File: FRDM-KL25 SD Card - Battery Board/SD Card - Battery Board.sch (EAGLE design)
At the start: 59 parts, among them U1 TPS63001, U2 TPS63002, U3 BQ27510DRZT-G3, U4 BQ24210DQCT

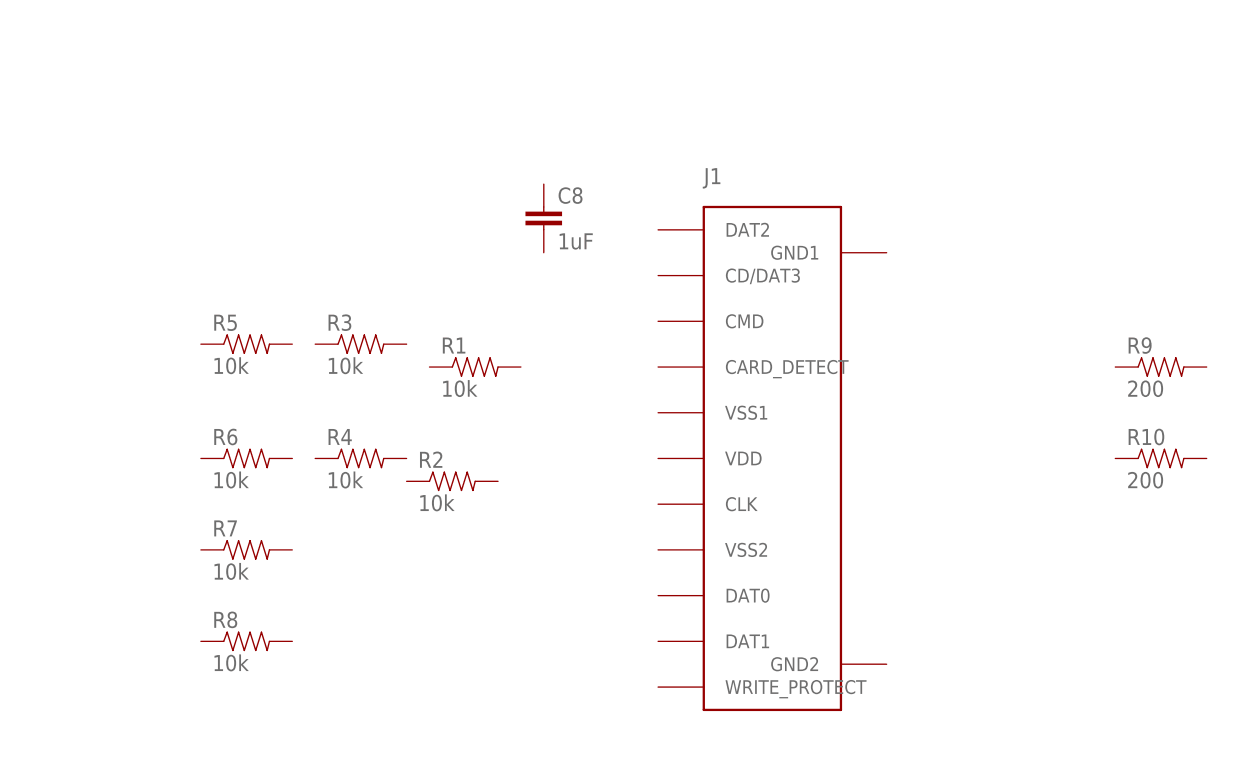
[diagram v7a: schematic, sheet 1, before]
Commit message: FRDM-KL25Z: Conected SD card circuit, nets have not been named
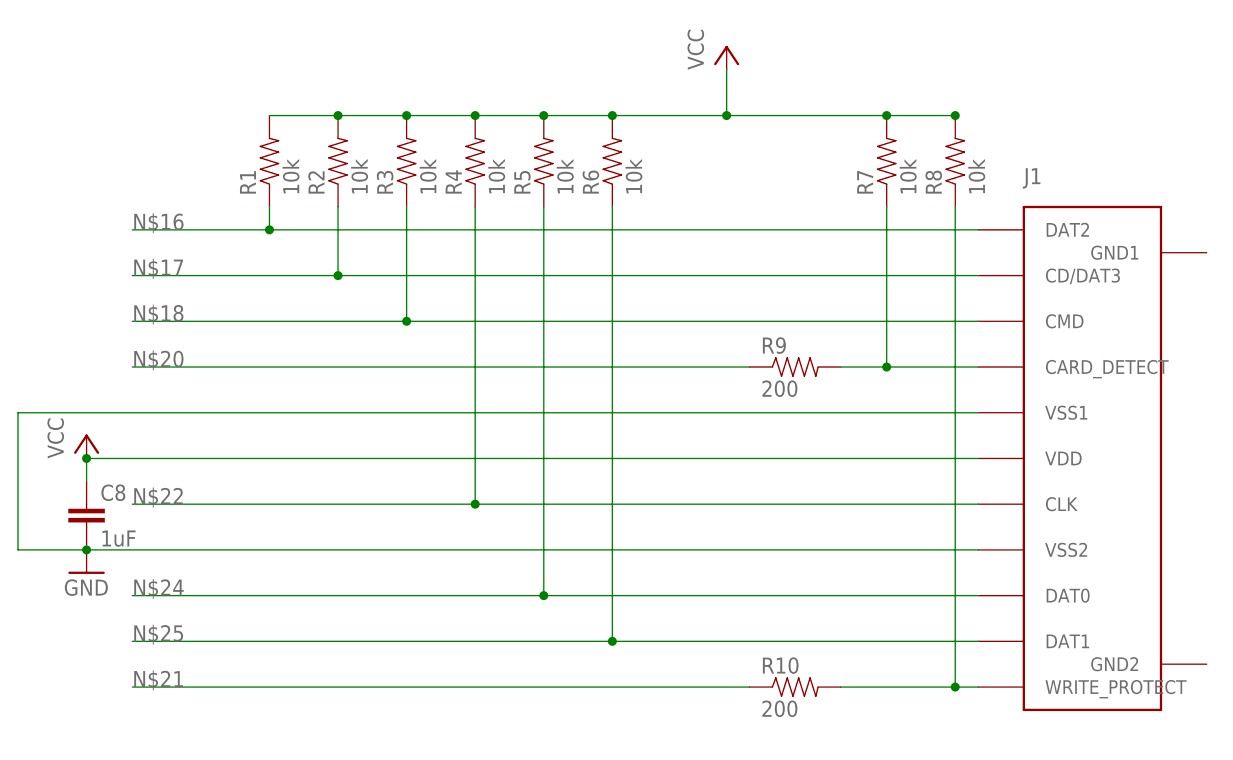
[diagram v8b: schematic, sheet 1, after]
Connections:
- new net N$16: J1.DAT2, R1.1
- new net N$17: J1.CD/DAT3, R2.1
- new net N$18: J1.CMD, R3.1
- new net N$19: J1.CARD_DETECT, R7.1, R9.2
- new net N$20: R9.1
- new net N$21: R10.1
- new net N$22: J1.CLK, R4.1
- new net N$24: J1.DAT0, R5.1
- new net N$25: J1.DAT1, R6.1
- new net N$26: J1.WRITE_PROTECT, R10.2, R8.1
- new net VCC: C8.1, J1.VDD, R1.2, R2.2, R3.2, R4.2, R5.2, R6.2, R7.2, R8.2
- net GND: now also C8.2, J1.VSS1, J1.VSS2
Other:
- moved on the sheet: C8, J1, R1, R10, R2, R3, R4, R5, R6, R7, R8, R9
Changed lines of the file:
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@@
 <part name="C13" library="Kas-Capacitors" deviceset="CAPACITOR" device="0.1U-X7R-10%-25V-0603" value="0.1uF"/>
 <part name="C14" library="Kas-Capacitors" deviceset="CAPACITOR" device="0.1U-X7R-10%-25V-0603" value="0.1uF"/>
+<part name="GND4" library="Kas-Pwr" deviceset="GND" device=""/>
+<part name="P+1" library="Kas-Pwr" deviceset="VCC" device=""/>
+<part name="P+2" library="Kas-Pwr" deviceset="VCC" device=""/>
 </parts>
 <sheets>
@@
 </plain>
 <instances>
-<instance part="R1" gate="G$1" x="25.4" y="63.5"/>
-<instance part="R2" gate="G$1" x="22.86" y="50.8"/>
-<instance part="R3" gate="G$1" x="12.7" y="66.04"/>
-<instance part="R4" gate="G$1" x="12.7" y="53.34"/>
-<instance part="R5" gate="G$1" x="0" y="66.04"/>
-<instance part="R6" gate="G$1" x="0" y="53.34"/>
-<instance part="R7" gate="G$1" x="0" y="43.18"/>
-<instance part="R8" gate="G$1" x="0" y="33.02"/>
-<instance part="R9" gate="G$1" x="101.6" y="63.5"/>
-<instance part="R10" gate="G$1" x="101.6" y="53.34"/>
-<instance part="J1" gate="G$1" x="58.42" y="58.42"/>
-<instance part="C8" gate="G$1" x="33.02" y="78.74"/>
+<instance part="R1" gate="G$1" x="2.54" y="86.36" rot="R90"/>
+<instance part="R2" gate="G$1" x="10.16" y="86.36" rot="R90"/>
+<instance part="R3" gate="G$1" x="17.78" y="86.36" rot="R90"/>
+<instance part="R4" gate="G$1" x="25.4" y="86.36" rot="R90"/>
+<instance part="R5" gate="G$1" x="33.02" y="86.36" rot="R90"/>
+<instance part="R6" gate="G$1" x="40.64" y="86.36" rot="R90"/>
+<instance part="R7" gate="G$1" x="71.12" y="86.36" rot="R90"/>
+<instance part="R8" gate="G$1" x="78.74" y="86.36" rot="R90"/>
+<instance part="R9" gate="G$1" x="60.96" y="63.5"/>
+<instance part="R10" gate="G$1" x="60.96" y="27.94"/>
+<instance part="J1" gate="G$1" x="93.98" y="58.42"/>
+<instance part="C8" gate="G$1" x="-17.78" y="45.72"/>
+<instance part="GND4" gate="1" x="-17.78" y="40.64"/>
+<instance part="P+1" gate="VCC" x="-17.78" y="55.88"/>
+<instance part="P+2" gate="VCC" x="53.34" y="99.06"/>
 </instances>
 <busses>
 </busses>
 <nets>
+<net name="N$16" class="0">
+<segment>
+<pinref part="J1" gate="G$1" pin="DAT2"/>
+<wire x1="81.28" y1="78.74" x2="2.54" y2="78.74" width="0.1524" layer="91"/>
+<pinref part="R1" gate="G$1" pin="1"/>
+<wire x1="2.54" y1="81.28" x2="2.54" y2="78.74" width="0.1524" layer="91"/>
+<junction x="2.54" y="78.74"/>
+<wire x1="2.54" y1="78.74" x2="-10.16" y2="78.74" width="0.1524" layer="91"/>
+<wire x1="-12.7" y1="78.74" x2="-10.16" y2="78.74" width="0.1524" layer="91"/>
+<label x="-12.7" y="78.74" size="1.778" layer="95"/>
+</segment>
+</net>
+<net name="N$17" class="0">
+<segment>
+<pinref part="J1" gate="G$1" pin="CD/DAT3"/>
+<wire x1="81.28" y1="73.66" x2="10.16" y2="73.66" width="0.1524" layer="91"/>
+<pinref part="R2" gate="G$1" pin="1"/>
+<wire x1="10.16" y1="73.66" x2="-12.7" y2="73.66" width="0.1524" layer="91"/>
+<wire x1="10.16" y1="81.28" x2="10.16" y2="73.66" width="0.1524" layer="91"/>
+<junction x="10.16" y="73.66"/>
+<label x="-12.7" y="73.66" size="1.778" layer="95"/>
+</segment>
+</net>
+<net name="N$18" class="0">
+<segment>
+<pinref part="J1" gate="G$1" pin="CMD"/>
+<wire x1="81.28" y1="68.58" x2="17.78" y2="68.58" width="0.1524" layer="91"/>
+<pinref part="R3" gate="G$1" pin="1"/>
+<wire x1="17.78" y1="68.58" x2="-12.7" y2="68.58" width="0.1524" layer="91"/>
+<wire x1="17.78" y1="81.28" x2="17.78" y2="68.58" width="0.1524" layer="91"/>
+<junction x="17.78" y="68.58"/>
+<label x="-12.7" y="68.58" size="1.778" layer="95"/>
+</segment>
+</net>
+<net name="N$19" class="0">
+<segment>
+<pinref part="J1" gate="G$1" pin="CARD_DETECT"/>
+<wire x1="81.28" y1="63.5" x2="71.12" y2="63.5" width="0.1524" layer="91"/>
+<pinref part="R9" gate="G$1" pin="2"/>
+<pinref part="R7" gate="G$1" pin="1"/>
+<wire x1="71.12" y1="63.5" x2="66.04" y2="63.5" width="0.1524" layer="91"/>
+<wire x1="71.12" y1="81.28" x2="71.12" y2="63.5" width="0.1524" layer="91"/>
+<junction x="71.12" y="63.5"/>
+</segment>
+</net>
+<net name="N$22" class="0">
+<segment>
+<pinref part="J1" gate="G$1" pin="CLK"/>
+<wire x1="81.28" y1="48.26" x2="25.4" y2="48.26" width="0.1524" layer="91"/>
+<pinref part="R4" gate="G$1" pin="1"/>
+<wire x1="25.4" y1="48.26" x2="-12.7" y2="48.26" width="0.1524" layer="91"/>
+<wire x1="25.4" y1="81.28" x2="25.4" y2="48.26" width="0.1524" layer="91"/>
+<junction x="25.4" y="48.26"/>
+<label x="-12.7" y="48.26" size="1.778" layer="95"/>
+</segment>
+</net>
+<net name="N$24" class="0">
+<segment>
+<pinref part="J1" gate="G$1" pin="DAT0"/>
+<wire x1="81.28" y1="38.1" x2="33.02" y2="38.1" width="0.1524" layer="91"/>
+<pinref part="R5" gate="G$1" pin="1"/>
+<wire x1="33.02" y1="38.1" x2="-12.7" y2="38.1" width="0.1524" layer="91"/>
+<wire x1="33.02" y1="81.28" x2="33.02" y2="38.1" width="0.1524" layer="91"/>
+<junction x="33.02" y="38.1"/>
+<label x="-12.7" y="38.1" size="1.778" layer="95"/>
+</segment>
+</net>
+<net name="N$25" class="0">
+<segment>
+<pinref part="J1" gate="G$1" pin="DAT1"/>
+<wire x1="81.28" y1="33.02" x2="40.64" y2="33.02" width="0.1524" layer="91"/>
+<pinref part="R6" gate="G$1" pin="1"/>
+<wire x1="40.64" y1="33.02" x2="-12.7" y2="33.02" width="0.1524" layer="91"/>
+<wire x1="40.64" y1="81.28" x2="40.64" y2="33.02" width="0.1524" layer="91"/>
+<junction x="40.64" y="33.02"/>
+<label x="-12.7" y="33.02" size="1.778" layer="95"/>
+</segment>
+</net>
+<net name="N$26" class="0">
+<segment>
+<pinref part="J1" gate="G$1" pin="WRITE_PROTECT"/>
+<wire x1="81.28" y1="27.94" x2="78.74" y2="27.94" width="0.1524" layer="91"/>
+<pinref part="R10" gate="G$1" pin="2"/>
+<pinref part="R8" gate="G$1" pin="1"/>
+<wire x1="78.74" y1="27.94" x2="66.04" y2="27.94" width="0.1524" layer="91"/>
+<wire x1="78.74" y1="81.28" x2="78.74" y2="27.94" width="0.1524" layer="91"/>
+<junction x="78.74" y="27.94"/>
+</segment>
+</net>
+<net name="GND" class="0">
+<segment>
+<pinref part="J1" gate="G$1" pin="VSS1"/>
+<wire x1="81.28" y1="58.42" x2="-25.4" y2="58.42" width="0.1524" layer="91"/>
+<wire x1="-25.4" y1="58.42" x2="-25.4" y2="43.18" width="0.1524" layer="91"/>
+<pinref part="J1" gate="G$1" pin="VSS2"/>
+<wire x1="81.28" y1="43.18" x2="-17.78" y2="43.18" width="0.1524" layer="91"/>
+<pinref part="C8" gate="G$1" pin="2"/>
+<wire x1="-25.4" y1="43.18" x2="-17.78" y2="43.18" width="0.1524" layer="91"/>
+<junction x="-17.78" y="43.18"/>
+<pinref part="GND4" gate="1" pin="GND"/>
+</segment>
+</net>
+<net name="VCC" class="0">
+<segment>
+<pinref part="J1" gate="G$1" pin="VDD"/>
+<wire x1="81.28" y1="53.34" x2="-17.78" y2="53.34" width="0.1524" layer="91"/>
+<pinref part="C8" gate="G$1" pin="1"/>
+<wire x1="-17.78" y1="53.34" x2="-17.78" y2="50.8" width="0.1524" layer="91"/>
+<pinref part="P+1" gate="VCC" pin="VCC"/>
+<junction x="-17.78" y="53.34"/>
+</segment>
+<segment>
+<pinref part="R1" gate="G$1" pin="2"/>
+<pinref part="R8" gate="G$1" pin="2"/>
+<wire x1="2.54" y1="91.44" x2="10.16" y2="91.44" width="0.1524" layer="91"/>
+<pinref part="R2" gate="G$1" pin="2"/>
+<junction x="10.16" y="91.44"/>
+<wire x1="10.16" y1="91.44" x2="17.78" y2="91.44" width="0.1524" layer="91"/>
+<pinref part="R3" gate="G$1" pin="2"/>
+<junction x="17.78" y="91.44"/>
+<wire x1="17.78" y1="91.44" x2="25.4" y2="91.44" width="0.1524" layer="91"/>
+<pinref part="R4" gate="G$1" pin="2"/>
+<junction x="25.4" y="91.44"/>
+<wire x1="25.4" y1="91.44" x2="33.02" y2="91.44" width="0.1524" layer="91"/>
+<pinref part="R5" gate="G$1" pin="2"/>
+<junction x="33.02" y="91.44"/>
+<wire x1="33.02" y1="91.44" x2="40.64" y2="91.44" width="0.1524" layer="91"/>
+<pinref part="R6" gate="G$1" pin="2"/>
+<junction x="40.64" y="91.44"/>
+<wire x1="40.64" y1="91.44" x2="53.34" y2="91.44" width="0.1524" layer="91"/>
+<pinref part="R7" gate="G$1" pin="2"/>
+<junction x="71.12" y="91.44"/>
+<wire x1="53.34" y1="91.44" x2="71.12" y2="91.44" width="0.1524" layer="91"/>
+<wire x1="71.12" y1="91.44" x2="78.74" y2="91.44" width="0.1524" layer="91"/>
+<junction x="78.74" y="91.44"/>
+<pinref part="P+2" gate="VCC" pin="VCC"/>
+<wire x1="53.34" y1="96.52" x2="53.34" y2="91.44" width="0.1524" layer="91"/>
+<junction x="53.34" y="91.44"/>
+</segment>
+</net>
+<net name="N$20" class="0">
+<segment>
+<pinref part="R9" gate="G$1" pin="1"/>
+<wire x1="55.88" y1="63.5" x2="-12.7" y2="63.5" width="0.1524" layer="91"/>
+<label x="-12.7" y="63.5" size="1.778" layer="95"/>
+</segment>
+</net>
+<net name="N$21" class="0">
+<segment>
+<pinref part="R10" gate="G$1" pin="1"/>
+<wire x1="55.88" y1="27.94" x2="-12.7" y2="27.94" width="0.1524" layer="91"/>
+<label x="-12.7" y="27.94" size="1.778" layer="95"/>
+</segment>
+</net>
 </nets>
 </sheet>
